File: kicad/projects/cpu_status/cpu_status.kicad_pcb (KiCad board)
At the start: 2 copper layers, 203.2 x 97.8 mm, 108 parts, among them J1 Control_signal_backplane, J2 Aux_connection, J3 Bus_connection, J4 MAR_content_in, J5 Conn_01x03_Male, J6 Conn_01x02_Female, U1 74HC245, U10 74HC04, U2 74HC245, U3 74HC245, U4 74HC245, U5 74HC245, U6 74HC245, U7 74HC245, U8 74HC245, U9 74HC126

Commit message: Tech checks on cpu status.
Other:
- board text added: "JLCJLCJLCJLC"
- board text added: "LED ~OE"
- board text removed: "~LED OE"
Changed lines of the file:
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@@
   (general
     (thickness 1.6)
-    (drawings 161)
+    (drawings 177)
     (tracks 1178)
     (zones 0)
@@
       (effects (font (size 1 1) (thickness 0.15)))
     )
-    (fp_text value 74HC245 (at 3.81 25.19 90) (layer F.Fab)
+    (fp_text value 74HC245 (at 3.81 25.908 90) (layer F.SilkS)
       (effects (font (size 1 1) (thickness 0.15)))
     )
@@
       (effects (font (size 1 1) (thickness 0.15)))
     )
-    (fp_text value 74HC04 (at 3.81 17.57 90) (layer F.Fab)
+    (fp_text value 74HC04 (at 3.81 18.034 90) (layer F.SilkS)
       (effects (font (size 1 1) (thickness 0.15)))
     )
@@
     (descr "C, Disc series, Radial, pin pitch=5.00mm, , diameter*width=4.7*2.5mm^2, Capacitor, http://www.vishay.com/docs/45233/krseries.pdf")
     (tags "C Disc series Radial pin pitch 5.00mm  diameter 4.7mm width 2.5mm Capacitor")
-    (fp_text reference C13 (at 2.5 -2.5 90) (layer F.SilkS)
+    (fp_text reference C13 (at 2.5 2.286 90) (layer F.SilkS)
       (effects (font (size 1 1) (thickness 0.15)))
     )
@@
     (descr "Through hole angled pin header, 1x32, 2.54mm pitch, 6mm pin length, single row")
     (tags "Through hole angled pin header THT 1x32 2.54mm single row")
-    (fp_text reference J1 (at 4.385 -2.27 90) (layer F.SilkS)
+    (fp_text reference J1 (at 2.54 -2.54 90) (layer F.SilkS)
       (effects (font (size 1 1) (thickness 0.15)))
     )
@@
     (descr "Through hole angled pin header, 1x16, 2.54mm pitch, 6mm pin length, single row")
     (tags "Through hole angled pin header THT 1x16 2.54mm single row")
-    (fp_text reference J3 (at 4.385 -2.27 90) (layer F.SilkS)
+    (fp_text reference J3 (at 2.54 -2.794 90) (layer F.SilkS)
       (effects (font (size 1 1) (thickness 0.15)))
     )
@@
     (descr "Through hole angled pin header, 1x10, 2.54mm pitch, 6mm pin length, single row")
     (tags "Through hole angled pin header THT 1x10 2.54mm single row")
-    (fp_text reference J2 (at 4.385 -2.27 90) (layer F.SilkS)
+    (fp_text reference J2 (at 2.54 -2.54 90) (layer F.SilkS)
       (effects (font (size 1 1) (thickness 0.15)))
     )
@@
       (effects (font (size 1 1) (thickness 0.15)))
     )
-    (fp_text value 74HC126 (at 3.81 17.57 90) (layer F.Fab)
+    (fp_text value 74HC126 (at 3.81 18.542 90) (layer F.SilkS)
       (effects (font (size 1 1) (thickness 0.15)))
     )
@@
       (effects (font (size 1 1) (thickness 0.15)))
     )
-    (fp_text value 74HC245 (at 3.81 25.19 90) (layer F.Fab)
+    (fp_text value 74HC245 (at 3.81 26.67 90) (layer F.SilkS)
       (effects (font (size 1 1) (thickness 0.15)))
     )
@@
       (effects (font (size 1 1) (thickness 0.15)))
     )
-    (fp_text value 74HC245 (at 3.81 25.19 90) (layer F.Fab)
+    (fp_text value 74HC245 (at 3.81 26.416 90) (layer F.SilkS)
       (effects (font (size 1 1) (thickness 0.15)))
     )
@@
       (effects (font (size 1 1) (thickness 0.15)))
     )
-    (fp_text value 74HC245 (at 3.81 25.19 90) (layer F.Fab)
+    (fp_text value 74HC245 (at 3.81 26.416 90) (layer F.SilkS)
       (effects (font (size 1 1) (thickness 0.15)))
     )
@@
       (effects (font (size 1 1) (thickness 0.15)))
     )
-    (fp_text value 74HC245 (at 3.81 25.19 90) (layer F.Fab)
+    (fp_text value 74HC245 (at 3.81 26.162 90) (layer F.SilkS)
       (effects (font (size 1 1) (thickness 0.15)))
     )
@@
       (effects (font (size 1 1) (thickness 0.15)))
     )
-    (fp_text value 74HC245 (at 3.81 25.19 90) (layer F.Fab)
+    (fp_text value 74HC245 (at 3.81 26.416 90) (layer F.SilkS)
       (effects (font (size 1 1) (thickness 0.15)))
     )
@@
       (effects (font (size 1 1) (thickness 0.15)))
     )
-    (fp_text value 74HC245 (at 3.81 25.19 90) (layer F.Fab)
+    (fp_text value 74HC245 (at 3.81 26.416 90) (layer F.SilkS)
       (effects (font (size 1 1) (thickness 0.15)))
     )
@@
       (effects (font (size 1 1) (thickness 0.15)))
     )
-    (fp_text value 74HC245 (at 3.81 25.19 90) (layer F.Fab)
+    (fp_text value 74HC245 (at 3.81 25.908 90) (layer F.SilkS)
       (effects (font (size 1 1) (thickness 0.15)))
     )
@@
     )
   )
+  (gr_text JLCJLCJLCJLC (at 227.33 133.35) (layer F.SilkS)
+    (effects (font (size 1.778 1.778) (thickness 0.2032)))
+  )
+  (gr_line (start 239.014 81.28) (end 240.03 81.28) (layer F.SilkS) (width 0.254))
+  (gr_line (start 239.014 87.884) (end 239.014 81.28) (layer F.SilkS) (width 0.254))
+  (gr_line (start 238.252 93.218) (end 239.776 93.218) (layer F.SilkS) (width 0.254))
+  (gr_line (start 239.014 88.646) (end 239.014 87.884) (layer F.SilkS) (width 0.254))
+  (gr_line (start 238.506 93.726) (end 239.522 93.726) (layer F.SilkS) (width 0.254))
+  (gr_line (start 239.014 92.202) (end 239.014 93.218) (layer F.SilkS) (width 0.254))
+  (gr_line (start 239.776 91.948) (end 238.252 91.44) (layer F.SilkS) (width 0.254))
+  (gr_line (start 238.76 94.234) (end 239.268 94.234) (layer F.SilkS) (width 0.254))
+  (gr_line (start 239.014 92.202) (end 239.776 91.948) (layer F.SilkS) (width 0.254))
+  (gr_line (start 239.776 88.9) (end 239.014 88.646) (layer F.SilkS) (width 0.254))
+  (gr_line (start 239.776 88.9) (end 238.252 89.408) (layer F.SilkS) (width 0.254))
+  (gr_line (start 238.252 90.424) (end 239.776 90.932) (layer F.SilkS) (width 0.254))
+  (gr_line (start 239.776 90.932) (end 238.252 91.44) (layer F.SilkS) (width 0.254))
+  (gr_line (start 239.776 89.916) (end 238.252 90.424) (layer F.SilkS) (width 0.254))
+  (gr_line (start 238.252 89.408) (end 239.776 89.916) (layer F.SilkS) (width 0.254))
   (gr_text 17 (at 243.84 66.548) (layer F.SilkS)
     (effects (font (size 1.27 1.27) (thickness 0.2032)))
@@
   (gr_line (start 244.348 87.376) (end 243.84 87.884) (layer F.SilkS) (width 0.254))
   (gr_line (start 244.348 92.964) (end 244.348 87.376) (layer F.SilkS) (width 0.254))
-  (gr_text "~LED OE" (at 248.666 90.678) (layer F.SilkS)
+  (gr_text "LED ~OE" (at 248.666 90.424) (layer F.SilkS)
     (effects (font (size 1.143 1.143) (thickness 0.1778)))
   )
@@
     (effects (font (size 1.524 1.524) (thickness 0.254)))
   )
-  (gr_text RESET (at 164.338 55.118) (layer F.SilkS)
+  (gr_text RESET (at 157.988 63.5) (layer F.SilkS)
     (effects (font (size 1.27 1.27) (thickness 0.2032)))
   )

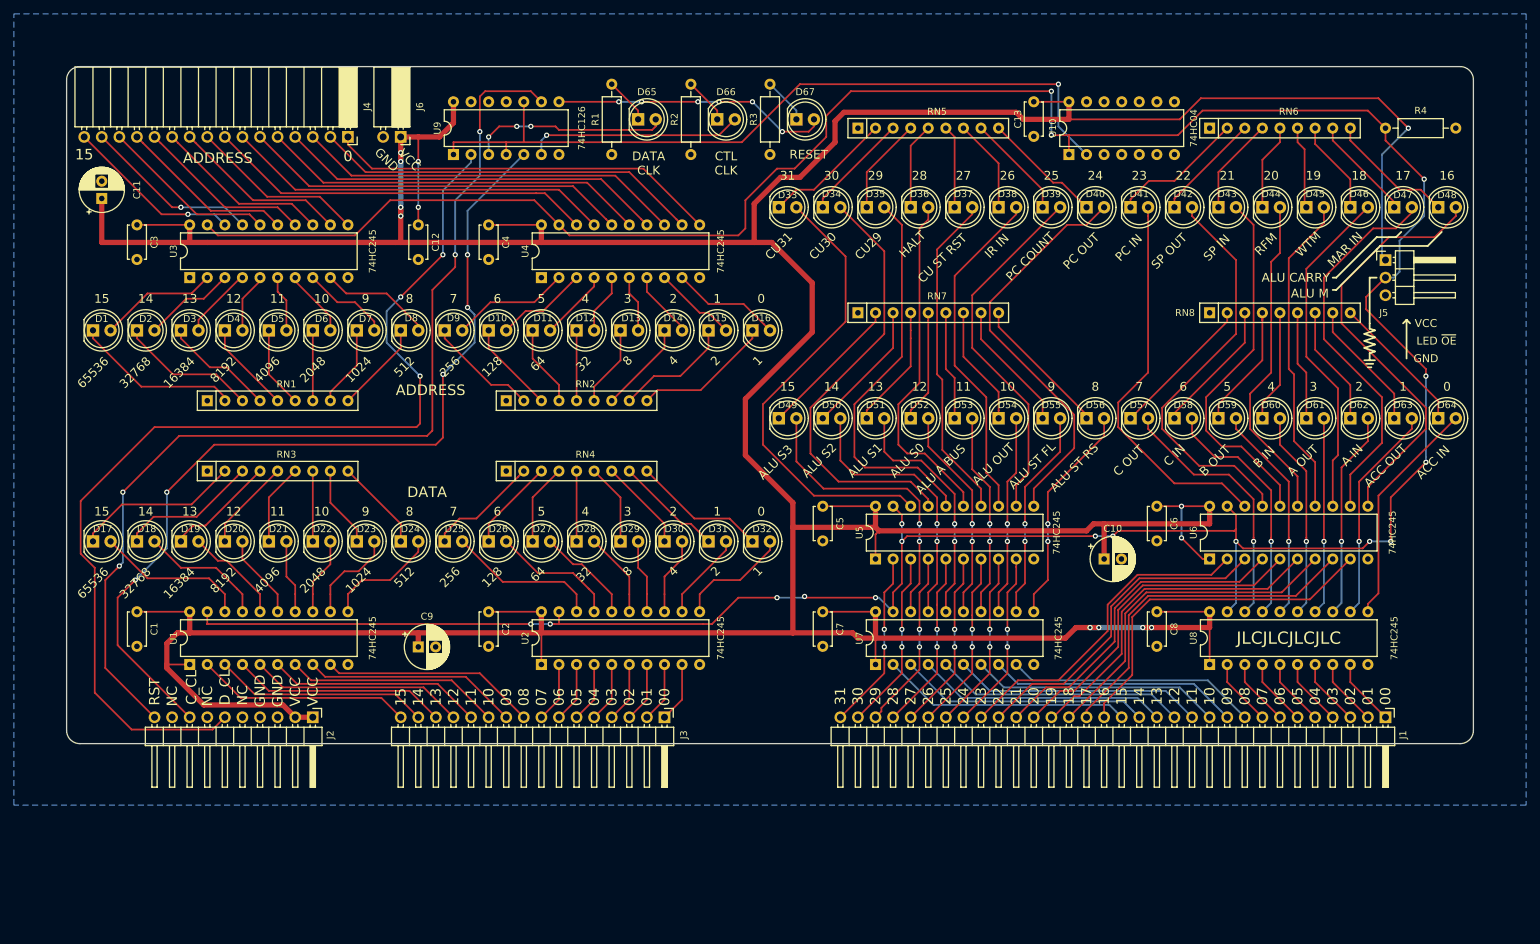
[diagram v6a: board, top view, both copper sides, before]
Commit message: Part way through adding ECNZ to status.
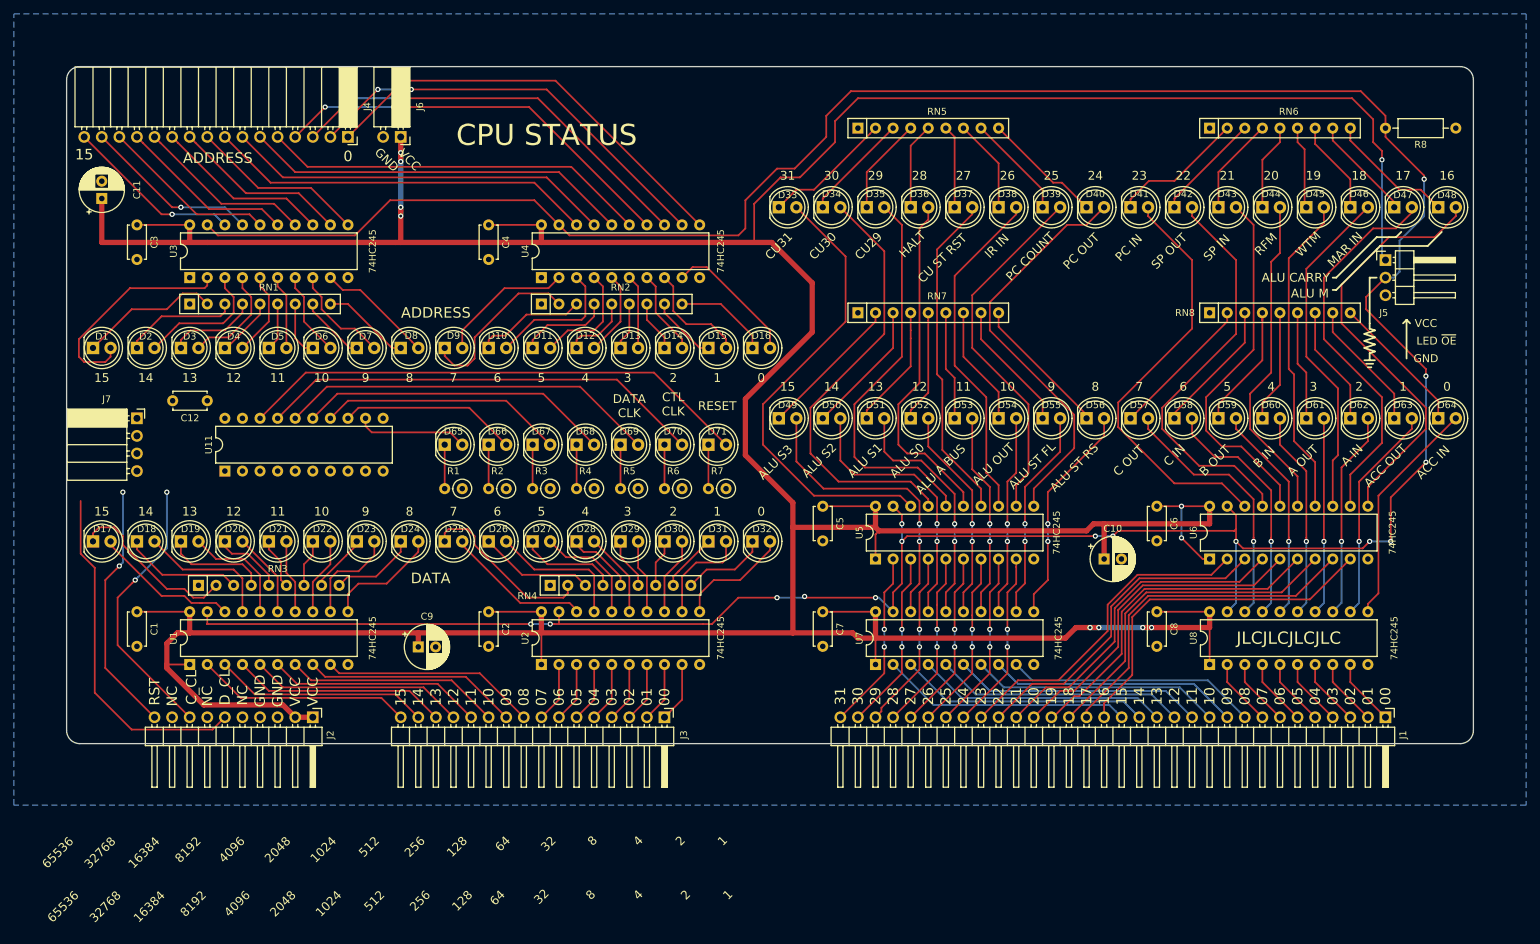
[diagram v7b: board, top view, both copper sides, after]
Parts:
- removed C13: 0.1uF, Capacitor_THT:C_Disc_D4.7mm_W2.5mm_P5.00mm
- removed U10: 74HC04, Package_DIP:DIP-14_W7.62mm
- removed U9: 74HC126, Package_DIP:DIP-14_W7.62mm
- added D68: LED, sixteen-bit-computer:LED_D5.0mm, F.Cu at (124.5, 105.4)
- added D69: LED, sixteen-bit-computer:LED_D5.0mm, F.Cu at (130.8, 105.4)
- added D70: LED, sixteen-bit-computer:LED_D5.0mm, F.Cu at (137.2, 105.4)
- added D71: LED, sixteen-bit-computer:LED_D5.0mm, F.Cu at (143.5, 105.4)
- added J7: Conn_01x04_Female, Connector_PinSocket_2.54mm:PinSocket_1x04_P2.54mm_Horizontal, F.Cu at (61.0, 101.6)
- added R5: 10K, Resistor_THT:R_Axial_DIN0207_L6.3mm_D2.5mm_P2.54mm_Vertical, F.Cu at (133.3, 111.8)
- added R6: 10K, Resistor_THT:R_Axial_DIN0207_L6.3mm_D2.5mm_P2.54mm_Vertical, F.Cu at (139.7, 111.8)
- added R7: 10K, Resistor_THT:R_Axial_DIN0207_L6.3mm_D2.5mm_P2.54mm_Vertical, F.Cu at (146.1, 111.8)
- added R8: 10K, Resistor_THT:R_Axial_DIN0207_L6.3mm_D2.5mm_P10.16mm_Horizontal, F.Cu at (251.5, 59.7)
- added U11: 74HC245, Package_DIP:DIP-20_W7.62mm, F.Cu at (73.7, 109.2)
- R1, R2: value 2K -> 10K; footprint Resistor_THT:R_Axial_DIN0207_L6.3mm_D2.5mm_P10.16mm_Horizontal -> Resistor_THT:R_Axial_DIN0207_L6.3mm_D2.5mm_P2.54mm_Vertical
- R3: value 1.3K -> 10K; footprint Resistor_THT:R_Axial_DIN0207_L6.3mm_D2.5mm_P10.16mm_Horizontal -> Resistor_THT:R_Axial_DIN0207_L6.3mm_D2.5mm_P2.54mm_Vertical
- R4: footprint Resistor_THT:R_Axial_DIN0207_L6.3mm_D2.5mm_P10.16mm_Horizontal -> Resistor_THT:R_Axial_DIN0207_L6.3mm_D2.5mm_P2.54mm_Vertical
- moved R4 134.9 mm to (127.0, 111.8)
- moved D67 60.5 mm to (118.1, 105.4)
- moved R3 57.8 mm to (120.7, 111.8), turned to 180 degrees
- moved D66 57.4 mm to (111.8, 105.4)
- moved R2 55.1 mm to (114.3, 111.8), turned to 180 degrees
- moved D65 54.7 mm to (105.4, 105.4)
- moved R1 52.9 mm to (108.0, 111.8), turned to 180 degrees
- moved C12 39.7 mm to (71.1, 99.1), turned to 180 degrees
- moved RN4 17.7 mm to (120.7, 125.7)
- moved RN3 16.6 mm to (69.8, 125.7)
- moved RN2 14.9 mm to (119.4, 85.1)
- moved RN1 14.2 mm to (68.6, 85.1)
- moved D1 2.54 mm to (54.6, 91.4)
- moved D10 2.54 mm to (111.8, 91.4)
- moved D11 2.54 mm to (118.1, 91.4)
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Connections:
- C12 pad 1: VCC -> Net-(C12-Pad1)
- C12 pad 2: GND -> Net-(C12-Pad2)
- D65 pad 2: /DATA_CLK_BUF -> Net-(D65-Pad2)
- D66 pad 2: /CTL_CLK_BUF -> Net-(D66-Pad2)
- D67 pad 2: /RESET_BUF -> Net-(D67-Pad2)
- R1 pad 1: GND -> Net-(R1-Pad1)
- R2 pad 1: GND -> Net-(R2-Pad1)
- R3 pad 1: GND -> Net-(R3-Pad1)
- R4 pad 1: GND -> Net-(R4-Pad1)
- R4 pad 2: /LED_CONTROL -> Net-(D68-Pad1)
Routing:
- net Net-(U10-Pad2): track 112.1 -> 0.00 mm, vias 1 -> 0
- net /RESET: track 145.8 -> 36.5 mm, vias 4 -> 2
- net /DATA_CLK: track 149.8 -> 50.3 mm, vias 3 -> 0
- net /CTL_CLK: track 129.5 -> 39.8 mm, vias 5 -> 2
- net Net-(D71-Pad2): track 0.00 -> 74.4 mm
- net Net-(D70-Pad2): track 0.00 -> 64.6 mm
- net Net-(D69-Pad2): track 0.00 -> 54.9 mm
- net Net-(D68-Pad2): track 0.00 -> 45.2 mm
- net /RESET_BUF: track 40.0 -> 0.00 mm, vias 6 -> 0
- net VCC: track 715.3 -> 677.2 mm, vias 13 -> 11
- net Net-(D67-Pad2): track 0.00 -> 35.4 mm
- net /CTL_CLK_BUF: track 31.2 -> 0.00 mm, vias 1 -> 0
- net /DATA_CLK_BUF: track 28.7 -> 0.00 mm, vias 3 -> 0
- net Net-(D66-Pad2): track 0.00 -> 25.7 mm
- net Net-(D65-Pad2): track 0.00 -> 16.2 mm
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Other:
- board text added: "CPU STATUS"

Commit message: Added ECNZ to CPU Status.
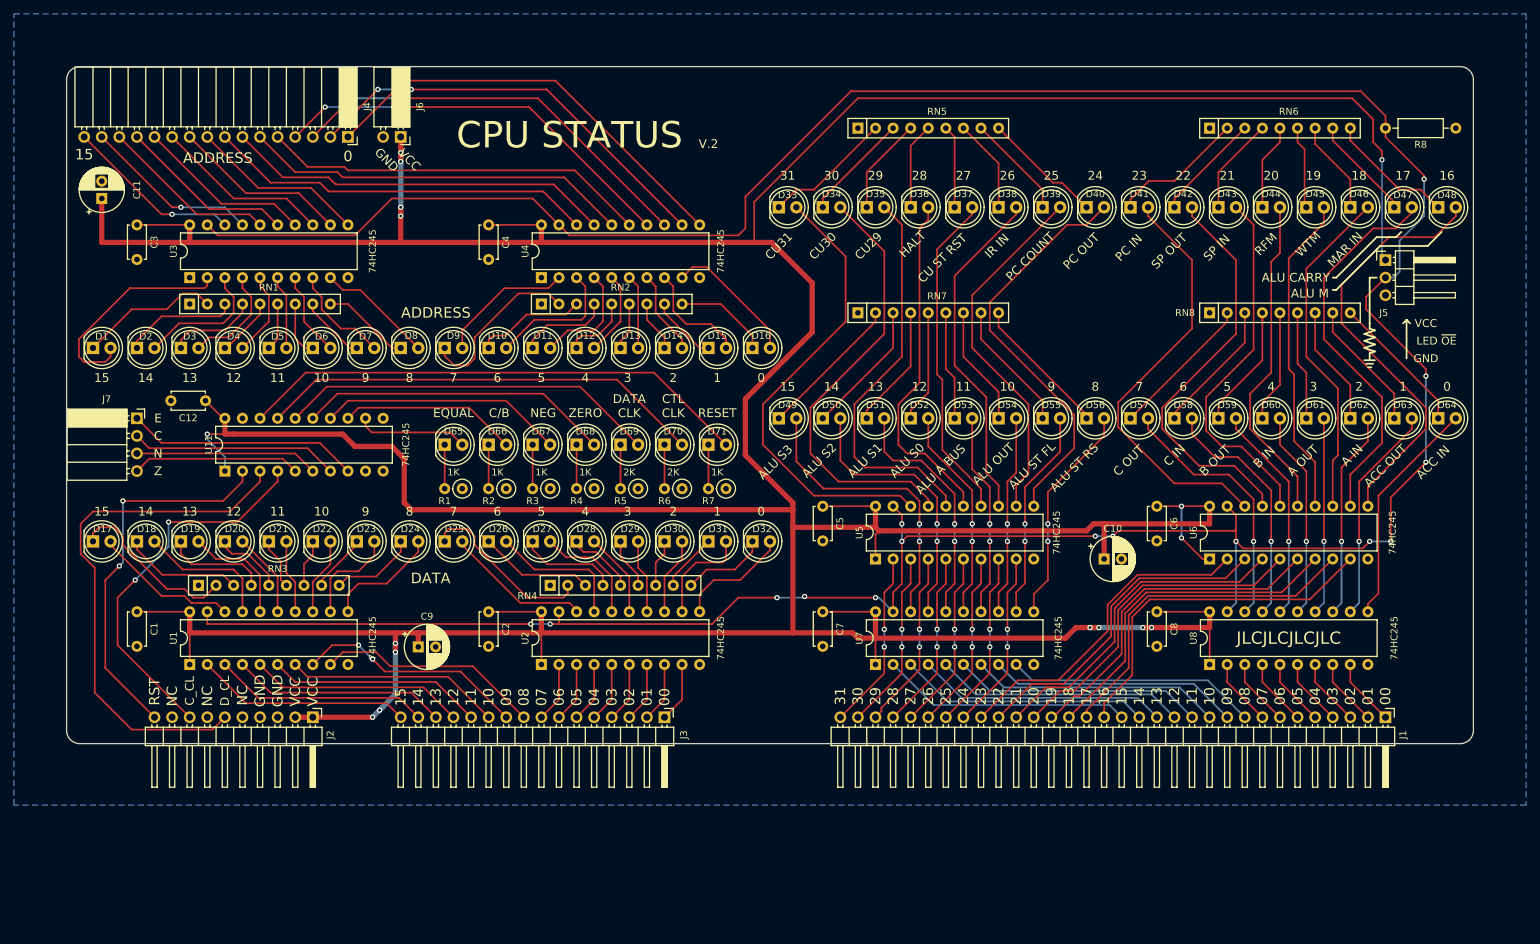
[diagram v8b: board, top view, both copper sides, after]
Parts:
- J7: value Conn_01x04_Female -> ECNZ
- R1, R2, R3, R4, R7: value 10K -> 1K
- R5, R6: value 10K -> 2K
- moved C12 0.25 mm to (70.9, 99.1)
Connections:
- C12 pad 1: Net-(C12-Pad1) -> VCC
- C12 pad 2: Net-(C12-Pad2) -> GND
- R1 pad 1: Net-(R1-Pad1) -> GND
- R2 pad 1: Net-(R2-Pad1) -> GND
- R3 pad 1: Net-(R3-Pad1) -> GND
- R4 pad 1: Net-(R4-Pad1) -> GND
- R5 pad 1: Net-(R5-Pad1) -> GND
- R6 pad 1: Net-(R6-Pad1) -> GND
- R7 pad 1: Net-(R7-Pad1) -> GND
- U11 pad 1: Net-(U11-Pad1) -> VCC
- U11 pad 10: Net-(U11-Pad10) -> GND
- U11 pad 2: Net-(U11-Pad2) -> /RESET
- U11 pad 20: Net-(U11-Pad20) -> VCC
- U11 pad 3: Net-(U11-Pad3) -> /DATA_CLK
- U11 pad 4: Net-(U11-Pad4) -> /CTL_CLK
- U11 pad 5: Net-(U11-Pad5) -> Net-(J7-Pad4)
- U11 pad 6: Net-(U11-Pad6) -> Net-(J7-Pad3)
- U11 pad 7: Net-(U11-Pad7) -> Net-(J7-Pad2)
- U11 pad 8: Net-(U11-Pad8) -> Net-(J7-Pad1)
- U11 pad 9: Net-(U11-Pad9) -> GND
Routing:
- net VCC: track 677.2 -> 776.7 mm, vias 11 -> 16
- net Net-(J7-Pad1): track 0.00 -> 33.9 mm
- net Net-(J7-Pad2): track 0.00 -> 30.0 mm
- net /DATA_CLK: track 50.3 -> 76.9 mm
- net Net-(J7-Pad3): track 0.00 -> 26.5 mm
- net Net-(J7-Pad4): track 0.00 -> 24.3 mm
- net /RESET: track 36.5 -> 55.2 mm
- net /CTL_CLK: track 39.8 -> 55.3 mm
- net /BUS_09: track 31.1 -> 33.4 mm, vias 0 -> 2
- net /BUS_08: track 31.1 -> 32.6 mm
- net /LED_CONTROL: track 472.9 -> 471.6 mm
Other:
- board text added: "C"
- board text added: "C/B"
- board text added: "E"
- board text added: "EQUAL"
- board text added: "N"
- board text added: "NEG"
- board text added: "V.2"
- board text added: "Z"
- board text added: "ZERO"
- board text removed: "1024"
- board text removed: "128"
- board text removed: "16384"
- board text removed: "2048"
- board text removed: "256"
- board text removed: "32"
- board text removed: "32768"
- board text removed: "4096"
- board text removed: "512"
- board text removed: "64"
- board text removed: "65536"
- board text removed: "8192"
